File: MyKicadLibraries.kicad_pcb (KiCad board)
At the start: 2 copper layers, 168.6 x 74.3 mm, 21 parts, among them J1 Conn_01x08, J2 Conn_01x08, J3 POGO Pins, J4 c8-inlet, J5 FTDI, J6 Micro_SD_Card, SW1 Schurter Switch, U1 radio-receiver, U10 rdm-6300, U11 magnetic-charger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

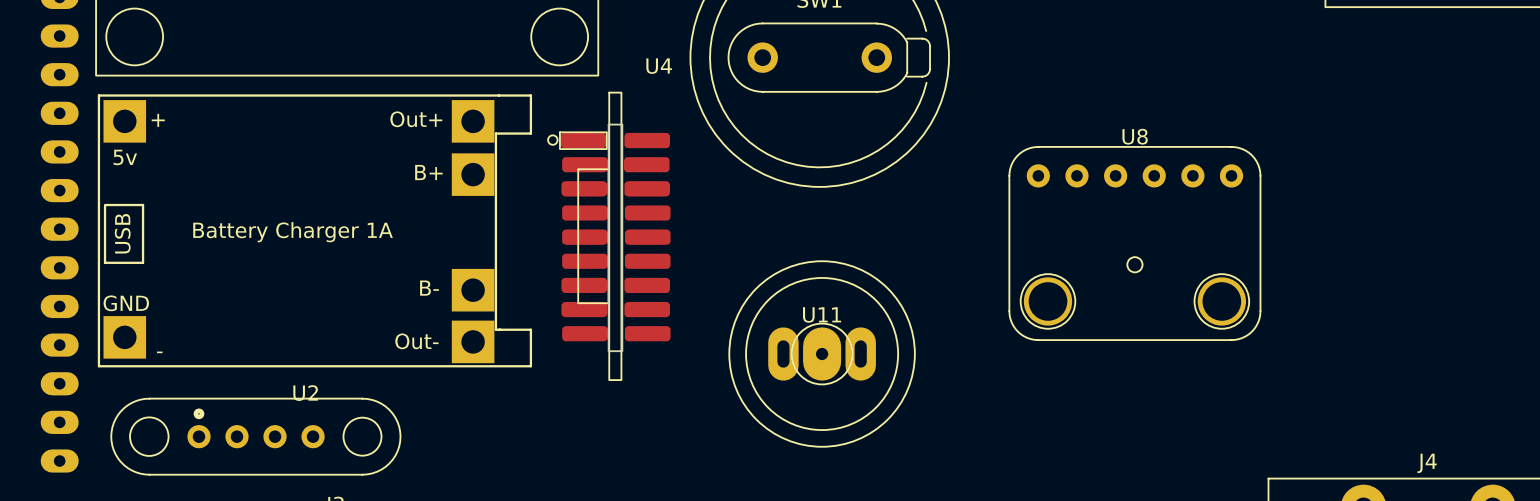
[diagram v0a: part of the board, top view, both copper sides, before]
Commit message: Update tp4056 footprint
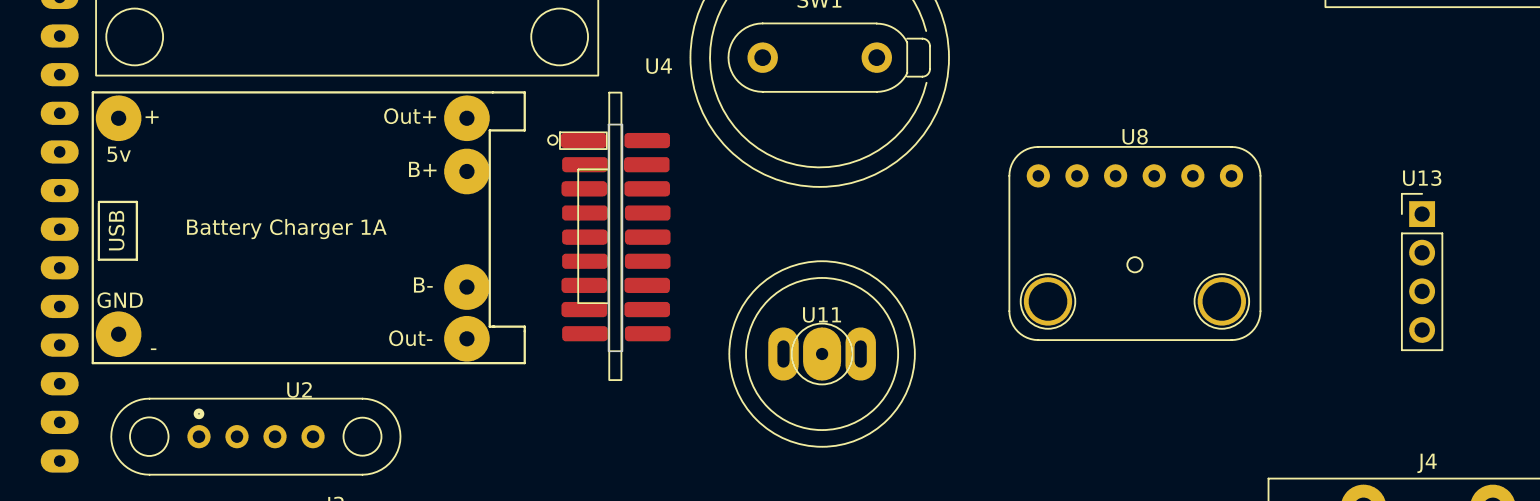
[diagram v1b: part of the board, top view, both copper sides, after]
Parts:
- added U13: TTL, Connector_PinHeader_2.54mm:PinHeader_1x04_P2.54mm_Vertical, F.Cu at (228.2, 66.8)
- moved U2 0.45 mm to (140.8, 58.8)

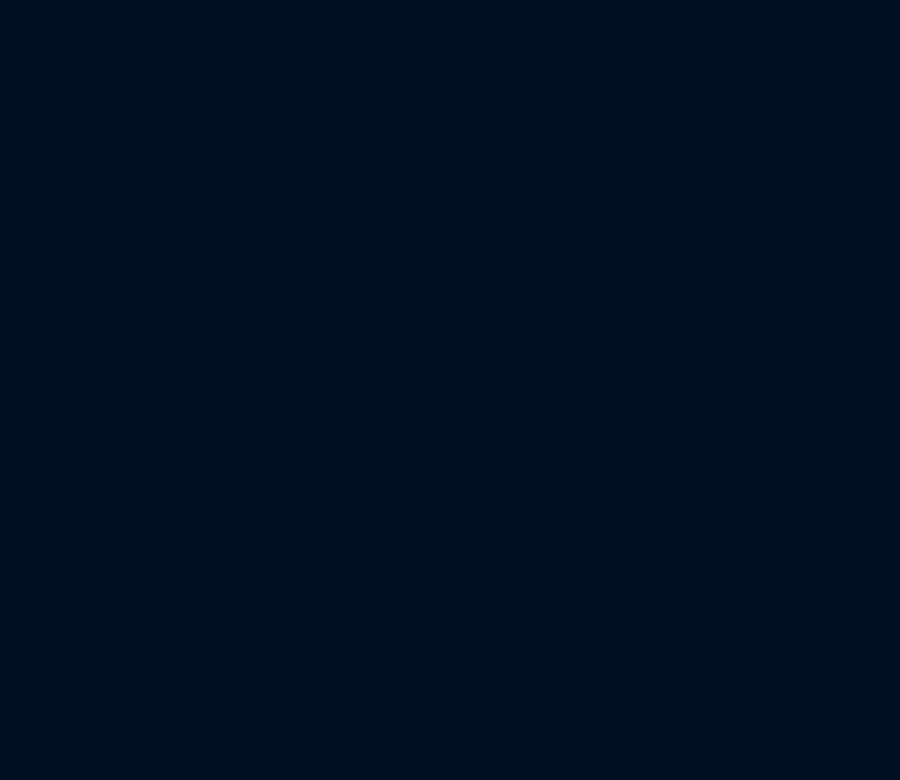
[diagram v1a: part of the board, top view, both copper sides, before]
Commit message: Add SOIC8 breakout
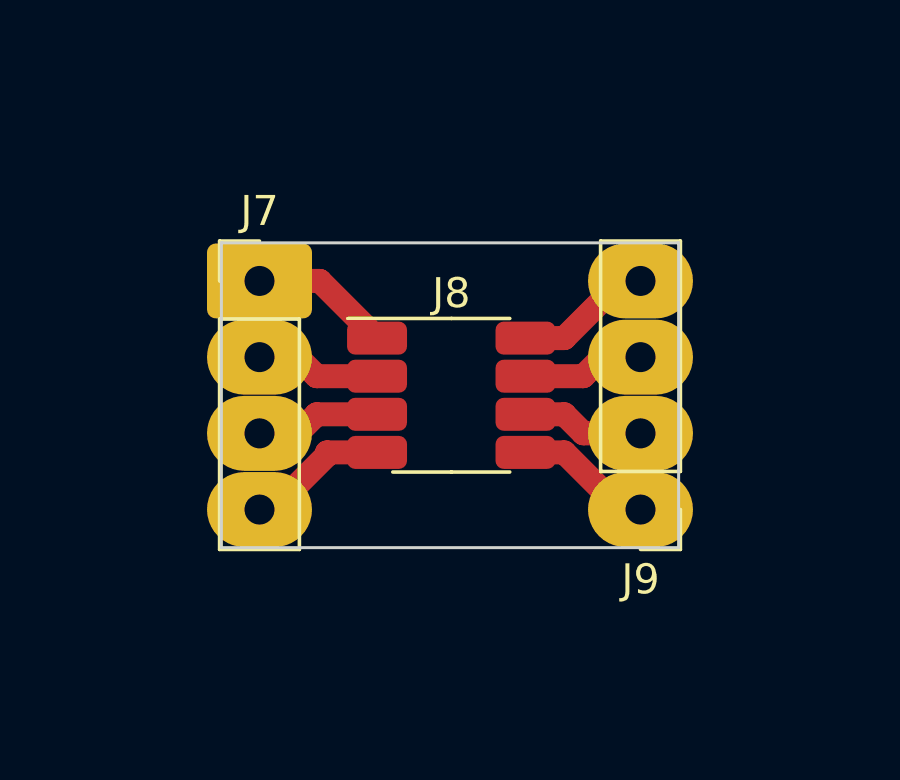
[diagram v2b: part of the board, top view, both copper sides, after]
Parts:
- added J7: Conn_01x04, Connector_PinHeader_2.54mm:PinHeader_1x04_P2.54mm_Vertical, F.Cu at (243.8, 114.3)
- added J8: Conn_02x04_Counter_Clockwise, Package_SO:SOIC-8_3.9x4.9mm_P1.27mm, F.Cu at (250.2, 118.1)
- added J9: Conn_01x04, Connector_PinHeader_2.54mm:PinHeader_1x04_P2.54mm_Vertical, F.Cu at (256.5, 121.9)
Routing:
- net Net-(J7-Pad4): track 0.00 -> 4.76 mm
- net Net-(J7-Pad1): track 0.00 -> 4.71 mm
- net Net-(J8-Pad8): track 0.00 -> 4.62 mm
- net Net-(J8-Pad5): track 0.00 -> 4.62 mm
- net Net-(J7-Pad3): track 0.00 -> 4.18 mm
- net Net-(J7-Pad2): track 0.00 -> 4.18 mm
- net Net-(J8-Pad7): track 0.00 -> 4.10 mm
- net Net-(J8-Pad6): track 0.00 -> 4.10 mm
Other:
- board size 168.6 x 74.3 mm -> 168.6 x 98.9 mm

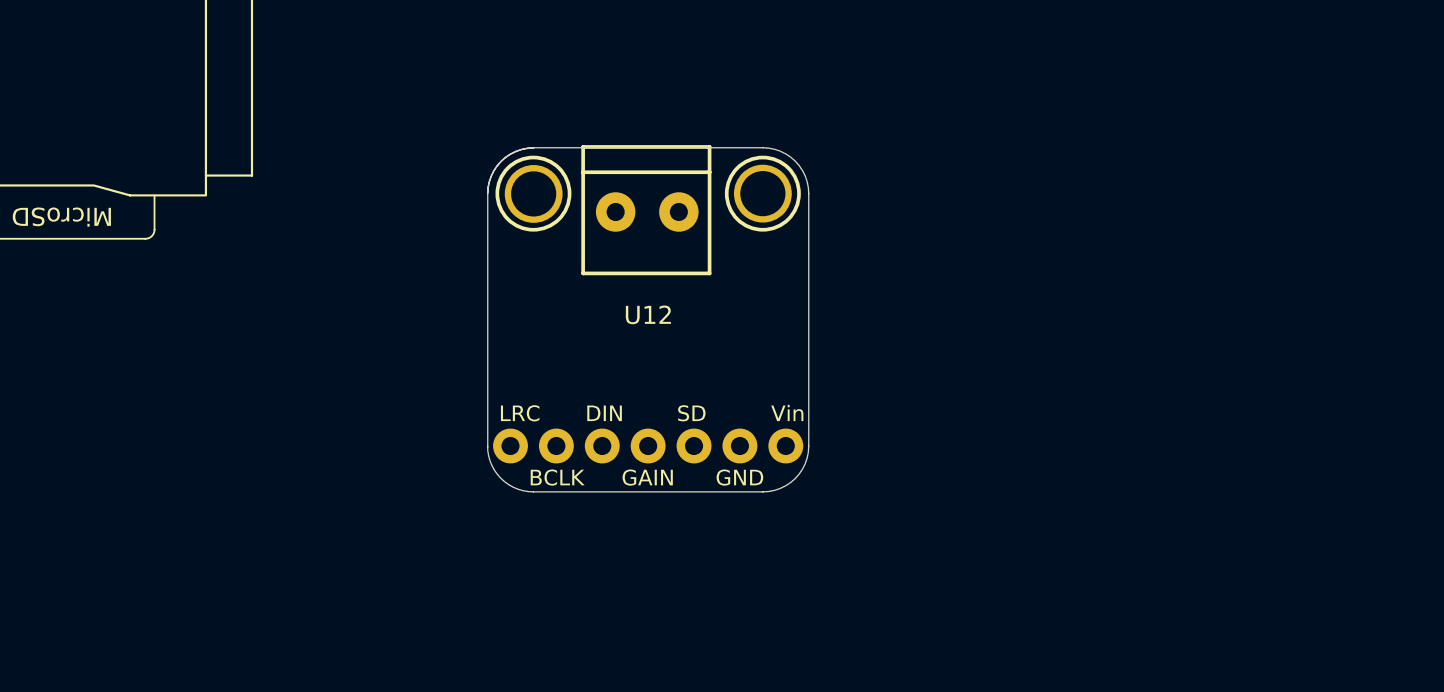
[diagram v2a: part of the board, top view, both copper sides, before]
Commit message: Add rcj-22 plug as well as lxb18 module
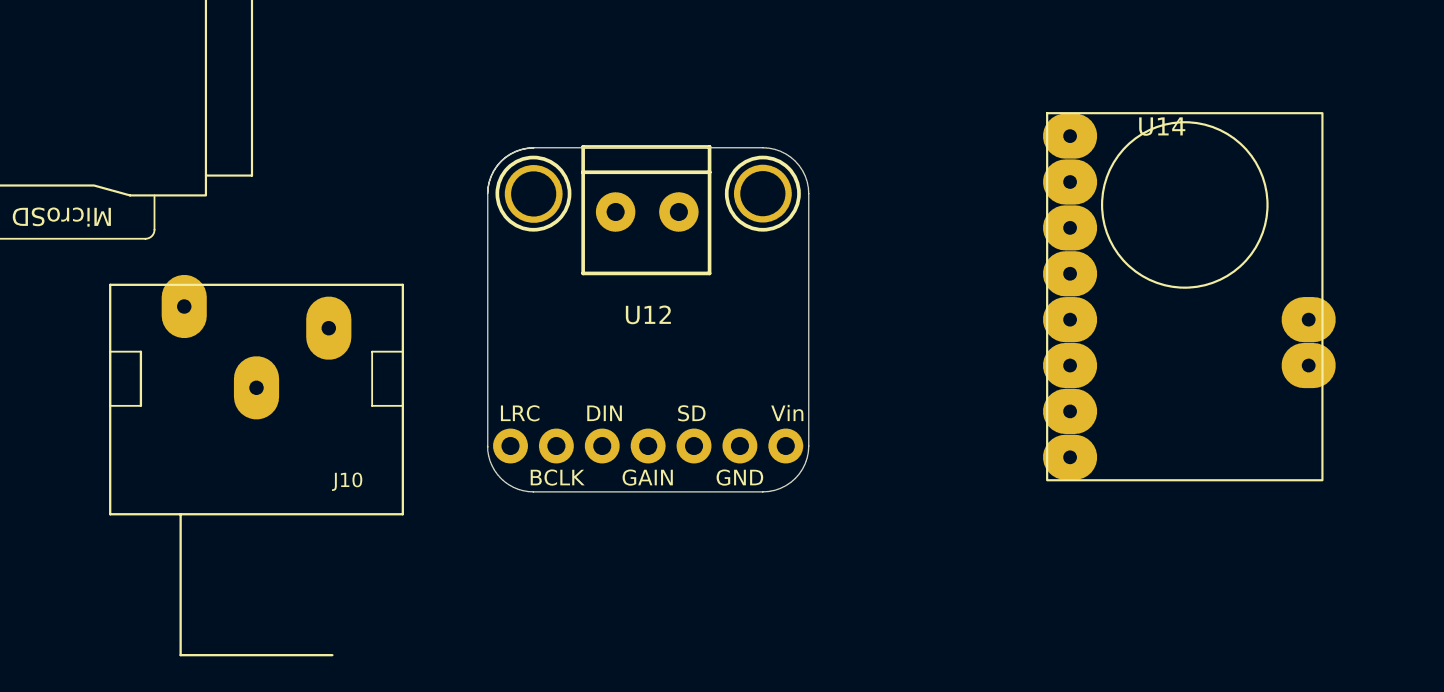
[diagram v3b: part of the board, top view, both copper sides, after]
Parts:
- added J10: RCJ-22, rcj-22:rcj-22, F.Cu at (170.0, 120.0)
- added U14: lxb18, lxb18:lxb18, F.Cu at (220.1, 109.1)
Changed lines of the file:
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@@
   (net 158 "Net-(J8-Pad7)")
   (net 159 "Net-(J8-Pad8)")
+  (net 160 "unconnected-(U14-Pad1)")
+  (net 161 "unconnected-(U14-Pad2)")
+  (net 162 "unconnected-(U14-Pad3)")
+  (net 163 "unconnected-(U14-Pad4)")
+  (net 164 "unconnected-(U14-Pad5)")
+  (net 165 "unconnected-(U14-Pad6)")
+  (net 166 "unconnected-(U14-Pad7)")
+  (net 167 "unconnected-(U14-Pad8)")
+  (net 168 "unconnected-(J10-Pad1)")
+  (net 169 "unconnected-(J10-Pad2)")
+  (net 170 "unconnected-(J10-Pad3)")
   (footprint "LilygoSimT7000:LilygoSIM7000G" (layer "F.Cu")
     (at 123.385 65.255)
@@
       (rotate (xyz 0 0 0))
     )
+  )
+  (footprint "lxb18:lxb18" (layer "F.Cu")
+    (at 220.1164 109.0676)
+    (property "Sheetfile" "MyKicadLibraries.kicad_sch")
+    (property "Sheetname" "")
+    (attr through_hole)
+    (fp_text reference "U14" (at 0 -0.5 unlocked) (layer "F.SilkS")
+      (effects (font (size 1 1) (thickness 0.15)))
+    )
+    (fp_text value "lxb18" (at 0 1 unlocked) (layer "F.Fab")
+      (effects (font (size 1 1) (thickness 0.15)))
+    )
+    (fp_text user "${REFERENCE}" (at 0 2.5 unlocked) (layer "F.Fab")
+      (effects (font (size 1 1) (thickness 0.15)))
+    )
+    (fp_rect (start -6.35 -1.27) (end 8.89 19.05) (layer "F.SilkS") (width 0.12) (fill none))
+    (fp_circle (center 1.27 3.81) (end 3.81 7.62) (layer "F.SilkS") (width 0.12) (fill none))
+    (pad "1" thru_hole oval (at -5.08 0) (size 3 2.5) (drill 0.762) (layers *.Cu *.Mask)
+      (net 160 "unconnected-(U14-Pad1)") (pinfunction "VCC") (pintype "input"))
+    (pad "2" thru_hole oval (at -5.08 7.62) (size 3 2.5) (drill 0.762) (layers *.Cu *.Mask)
+      (net 161 "unconnected-(U14-Pad2)") (pinfunction "GND") (pintype "input"))
+    (pad "2" thru_hole oval (at -5.08 2.54) (size 3 2.5) (drill 0.762) (layers *.Cu *.Mask)
+      (net 161 "unconnected-(U14-Pad2)") (pinfunction "GND") (pintype "input"))
+    (pad "2" thru_hole oval (at -5.08 5.08) (size 3 2.5) (drill 0.762) (layers *.Cu *.Mask)
+      (net 161 "unconnected-(U14-Pad2)") (pinfunction "GND") (pintype "input"))
+    (pad "3" thru_hole oval (at -5.08 10.16) (size 3 2.5) (drill 0.762) (layers *.Cu *.Mask)
+      (net 162 "unconnected-(U14-Pad3)") (pinfunction "Rec") (pintype "input"))
+    (pad "4" thru_hole oval (at -5.08 12.7) (size 3 2.5) (drill 0.762) (layers *.Cu *.Mask)
+      (net 163 "unconnected-(U14-Pad4)") (pinfunction "Play") (pintype "input"))
+    (pad "5" thru_hole oval (at -5.08 15.24) (size 3 2.5) (drill 0.762) (layers *.Cu *.Mask)
+      (net 164 "unconnected-(U14-Pad5)") (pinfunction "Mic-") (pintype "input"))
+    (pad "6" thru_hole oval (at -5.08 17.78) (size 3 2.5) (drill 0.762) (layers *.Cu *.Mask)
+      (net 165 "unconnected-(U14-Pad6)") (pinfunction "Mic+") (pintype "input"))
+    (pad "7" thru_hole oval (at 8.128 12.7) (size 3 2.5) (drill 0.762) (layers *.Cu *.Mask)
+      (net 166 "unconnected-(U14-Pad7)") (pinfunction "Speaker-") (pintype "input"))
+    (pad "8" thru_hole oval (at 8.128 10.16) (size 3 2.5) (drill 0.762) (layers *.Cu *.Mask)
+      (net 167 "unconnected-(U14-Pad8)") (pinfunction "Speaker+") (pintype "input"))
   )
   (footprint "magnetic-charger:magnetic-charger" (layer "F.Cu")
@@
     )
   )
+  (footprint "rcj-22:rcj-22" (layer "F.Cu")
+    (at 170 120 180)
+    (property "Sheetfile" "MyKicadLibraries.kicad_sch")
+    (property "Sheetname" "")
+    (attr through_hole)
+    (fp_text reference "J10" (at -5.08 -8.128) (layer "F.SilkS")
+      (effects (font (size 0.787402 0.787402) (thickness 0.15)))
+    )
+    (fp_text value "RCJ-22" (at 4.826 -8.382) (layer "F.Fab") hide
+      (effects (font (size 0.787402 0.787402) (thickness 0.15)))
+    )
+    (fp_line (start 6.4 -4) (end 6.4 -1) (layer "F.SilkS") (width 0.127))
+    (fp_line (start -8.1 2.7) (end 8.1 2.7) (layer "F.SilkS") (width 0.127))
+    (fp_line (start 8.1 -10) (end -8.1 -10) (layer "F.SilkS") (width 0.127))
+    (fp_line (start -8.1 -1) (end -6.4 -1) (layer "F.SilkS") (width 0.1))
+    (fp_line (start 4.2 -17.8) (end 4.2 -10) (layer "F.SilkS") (width 0.127))
+    (fp_line (start -8.1 -1) (end -8.1 2.7) (layer "F.SilkS") (width 0.127))
+    (fp_line (start 8.1 -4) (end 6.4 -4) (layer "F.SilkS") (width 0.1))
+    (fp_line (start -8.1 -4) (end -8.1 -1) (layer "F.SilkS") (width 0.127))
+    (fp_line (start -6.4 -1) (end -6.4 -4) (layer "F.SilkS") (width 0.1))
+    (fp_line (start -4.2 -17.8) (end 4.2 -17.8) (layer "F.SilkS") (width 0.127))
+    (fp_line (start 8.1 2.7) (end 8.1 -10) (layer "F.SilkS") (width 0.127))
+    (fp_line (start -8.1 -10) (end -8.1 -4) (layer "F.SilkS") (width 0.127))
+    (fp_line (start 8.1 -1) (end 8.1 -4) (layer "F.SilkS") (width 0.1))
+    (fp_line (start 6.4 -1) (end 8.1 -1) (layer "F.SilkS") (width 0.1))
+    (fp_line (start -6.4 -4) (end -8.1 -4) (layer "F.SilkS") (width 0.1))
+    (fp_line (start -4.7 -10) (end -4.2 -10) (layer "F.Fab") (width 0.127))
+    (fp_line (start -4.2 -10) (end -4.2 -17.8) (layer "F.Fab") (width 0.127))
+    (pad "" np_thru_hole oval (at 7.2 -2.5 180) (size 2 3.2) (drill oval 2 3.2) (layers F&B.Cu *.Mask))
+    (pad "" np_thru_hole oval (at -7.3 -2.5 180) (size 2 3.2) (drill oval 2 3.2) (layers F&B.Cu *.Mask))
+    (pad "1" thru_hole oval (at 0 -3 270) (size 3.5 2.5) (drill 0.8) (layers *.Cu *.Mask)
+      (net 168 "unconnected-(J10-Pad1)") (pinfunction "GND") (pintype "bidirectional"))
+    (pad "2" thru_hole oval (at -4 0.3 270) (size 3.5 2.5) (drill 0.8) (layers *.Cu *.Mask)
+      (net 169 "unconnected-(J10-Pad2)") (pinfunction "BTM") (pintype "bidirectional"))
+    (pad "3" thru_hole oval (at 4 1.5 270) (size 3.5 2.5) (drill 0.8) (layers *.Cu *.Mask)
+      (net 170 "unconnected-(J10-Pad3)") (pinfunction "TOP") (pintype "bidirectional"))
+    (model "${KIPRJMOD}/lib/rcj-22/rcj-22.step"
+      (offset (xyz 0 8.5 14.5))
+      (scale (xyz 1 1 1))
+      (rotate (xyz -90 0 180))
+    )
+  )
